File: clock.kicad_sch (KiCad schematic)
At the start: 24 parts, among them SW1 TL2230, U1 LM555, U2 74LS00, U3 LM555

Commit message: Modofied power flags and other minor edits.
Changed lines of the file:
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@@
     (rev "${version}")
-  )
-  (junction (at 107.95 50.8) (diameter 0) (color 0 0 0 0)
   )
   (junction (at 146.05 99.06) (diameter 0) (color 0 0 0 0)
@@
     (stroke (width 0) (type default))
   )
-  (wire (pts (xy 107.95 50.8) (xy 107.95 66.04))
+  (wire (pts (xy 107.95 46.99) (xy 107.95 66.04))
     (stroke (width 0) (type default))
   )
@@
     (stroke (width 0) (type default))
   )
-  (wire (pts (xy 107.95 46.99) (xy 107.95 50.8))
-    (stroke (width 0) (type default))
-  )
   (wire (pts (xy 29.21 81.28) (xy 29.21 104.14))
     (stroke (width 0) (type default))
@@
   )
   (wire (pts (xy 29.21 124.46) (xy 31.75 124.46))
-    (stroke (width 0) (type default))
-  )
-  (wire (pts (xy 107.95 50.8) (xy 110.49 50.8))
     (stroke (width 0) (type default))
   )
@@
         )
       )
-    )
-  )
-  (symbol (lib_id "power:PWR_FLAG") (at 110.49 50.8 270) (unit 1)
-    (in_bom yes) (on_board yes) (dnp no) (fields_autoplaced)
-    (property "Reference" "#FLG01" (at 112.395 50.8 0)
-      (effects (font (size 1 1)) hide)
-    )
-    (property "Value" "PWR_FLAG" (at 113.665 50.8 90)
-      (effects (font (size 1 1)) (justify left))
-    )
-    (property "Footprint" "" (at 110.49 50.8 0)
-      (effects (font (size 1 1)) hide)
-    )
-    (property "Datasheet" "~" (at 110.49 50.8 0)
-      (effects (font (size 1 1)) hide)
-    )
-    (pin "1")
-    (instances
-      (project "cpu"
-        (path "/7aab8e99-eed8-4c64-b2cd-ed9d372ca98a/acfbf03f-1d84-4836-b0c1-074c009b36ca"
-          (reference "#FLG01") (unit 1)
-        )
-      )

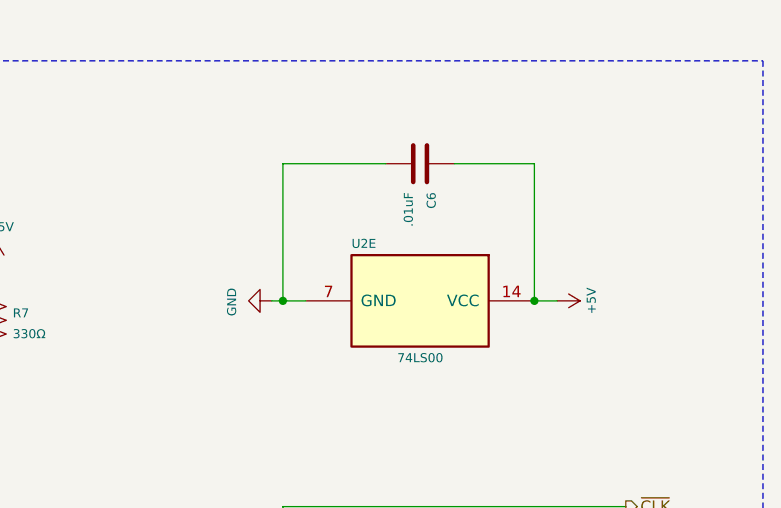
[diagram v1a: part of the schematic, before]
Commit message: Changed out USB connector for new power-only version with fewer pins. Generated new gerber/drill files.
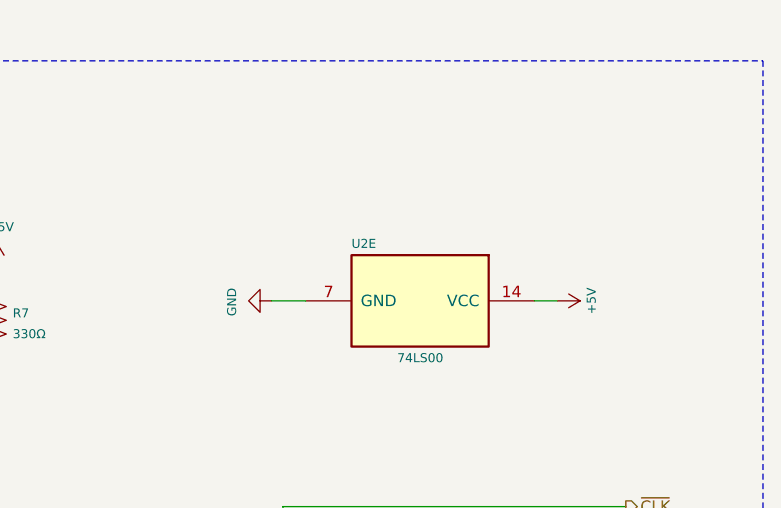
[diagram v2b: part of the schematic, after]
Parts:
- removed C6: .01uF, Capacitor_THT:C_Disc_D4.7mm_W2.5mm_P5.00mm, symbol Device:C
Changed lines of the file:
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@@
   (junction (at 29.21 81.28) (diameter 0) (color 0 0 0 0)
   )
-  (junction (at 237.49 50.8) (diameter 0) (color 0 0 0 0)
-  )
   (junction (at 191.77 134.62) (diameter 0) (color 0 0 0 0)
   )
@@
   )
   (junction (at 34.29 68.58) (diameter 0) (color 0 0 0 0)
-  )
-  (junction (at 209.55 50.8) (diameter 0) (color 0 0 0 0)
   )
   (no_connect (at 134.62 138.43))
@@
     (stroke (width 0) (type default))
   )
-  (wire (pts (xy 208.28 50.8) (xy 209.55 50.8))
+  (wire (pts (xy 208.28 50.8) (xy 212.09 50.8))
     (stroke (width 0) (type default))
   )
@@
     (stroke (width 0) (type default))
   )
-  (wire (pts (xy 220.98 35.56) (xy 209.55 35.56))
-    (stroke (width 0) (type default))
-  )
   (wire (pts (xy 146.05 121.92) (xy 146.05 99.06))
     (stroke (width 0) (type default))
   )
-  (wire (pts (xy 237.49 35.56) (xy 237.49 50.8))
-    (stroke (width 0) (type default))
-  )
   (wire (pts (xy 209.55 73.66) (xy 209.55 91.44))
     (stroke (width 0) (type default))
@@
     (stroke (width 0) (type default))
   )
-  (wire (pts (xy 209.55 50.8) (xy 212.09 50.8))
-    (stroke (width 0) (type default))
-  )
   (wire (pts (xy 69.85 81.28) (xy 72.39 81.28))
     (stroke (width 0) (type default))
@@
     (stroke (width 0) (type default))
   )
-  (wire (pts (xy 228.6 35.56) (xy 237.49 35.56))
-    (stroke (width 0) (type default))
-  )
   (wire (pts (xy 170.18 115.57) (xy 191.77 115.57))
     (stroke (width 0) (type default))
@@
   )
   (wire (pts (xy 191.77 83.82) (xy 191.77 81.28))
-    (stroke (width 0) (type default))
-  )
-  (wire (pts (xy 209.55 35.56) (xy 209.55 50.8))
     (stroke (width 0) (type default))
   )
@@
         )
       )
-    )
-  )
-  (symbol (lib_id "Device:C") (at 224.79 35.56 270) (unit 1)
-    (in_bom yes) (on_board yes) (dnp no) (fields_autoplaced)
-    (property "Reference" "C6" (at 226.06 38.735 0)
-      (effects (font (size 1 1)) (justify left))
-    )
-    (property "Value" ".01uF" (at 223.52 38.735 0)
-      (effects (font (size 1 1)) (justify left))
-    )
-    (property "Footprint" "Capacitor_THT:C_Disc_D4.7mm_W2.5mm_P5.00mm" (at 220.98 36.5252 0)
-      (effects (font (size 1 1)) hide)
-    )
-    (property "Datasheet" "~" (at 224.79 35.56 0)
-      (effects (font (size 1 1)) hide)
-    )
-    (pin "1")
-    (pin "2")
-    (instances
-      (project "cpu"
-        (path "/7aab8e99-eed8-4c64-b2cd-ed9d372ca98a/acfbf03f-1d84-4836-b0c1-074c009b36ca"
-          (reference "C6") (unit 1)
-        )
-      )

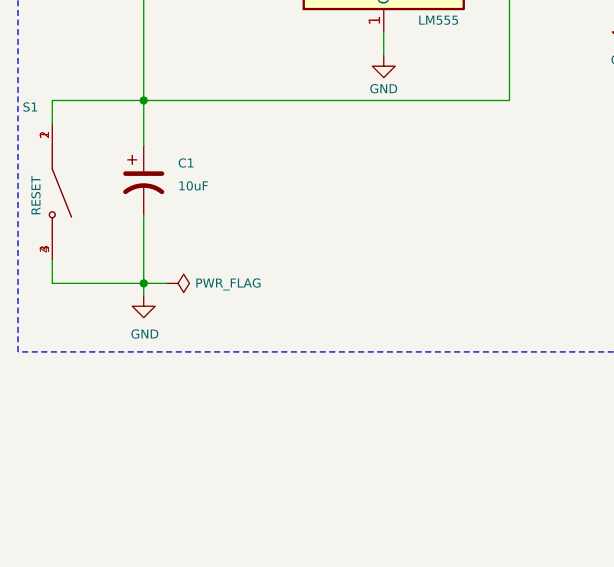
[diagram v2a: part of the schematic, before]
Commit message: Updated symbols/footprint for USB and 5K Trimmer Pots.
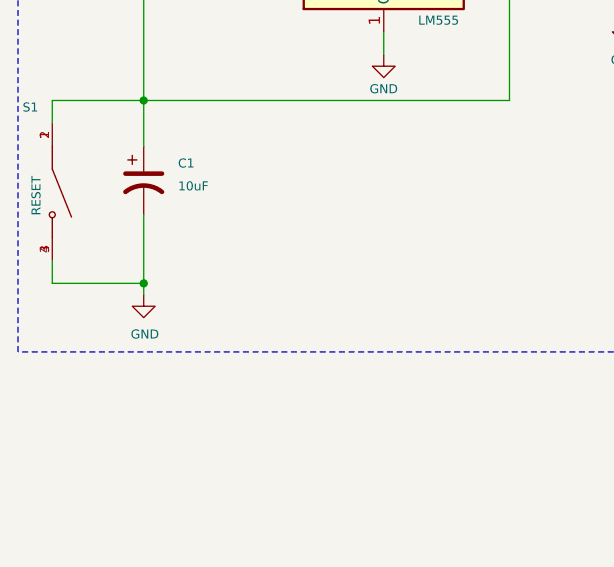
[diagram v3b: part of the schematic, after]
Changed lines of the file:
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@@
-    (stroke (width 0) (type default))
-  )
-  (wire (pts (xy 29.21 124.46) (xy 31.75 124.46))
     (stroke (width 0) (type default))
   )
@@
         )
       )
-    )
-  )
-  (symbol (lib_id "power:PWR_FLAG") (at 31.75 124.46 270) (unit 1)
-    (in_bom yes) (on_board yes) (dnp no) (fields_autoplaced)
-    (property "Reference" "#FLG02" (at 33.655 124.46 0)
-      (effects (font (size 1 1)) hide)
-    )
-    (property "Value" "PWR_FLAG" (at 34.925 124.46 90)
-      (effects (font (size 1 1)) (justify left))
-    )
-    (property "Footprint" "" (at 31.75 124.46 0)
-      (effects (font (size 1 1)) hide)
-    )
-    (property "Datasheet" "~" (at 31.75 124.46 0)
-      (effects (font (size 1 1)) hide)
-    )
-    (pin "1")
-    (instances
-      (project "cpu"
-        (path "/7aab8e99-eed8-4c64-b2cd-ed9d372ca98a/acfbf03f-1d84-4836-b0c1-074c009b36ca"
-          (reference "#FLG02") (unit 1)
-        )
-      )

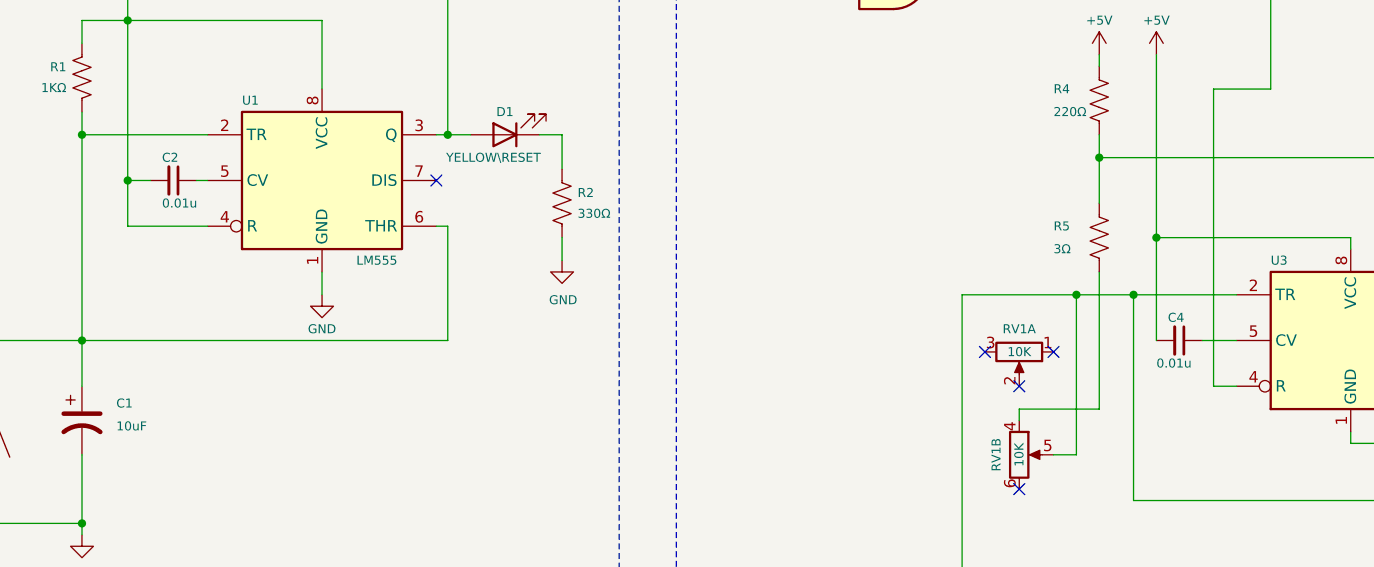
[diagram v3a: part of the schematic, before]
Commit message: Final changes around adding BOM to README.md
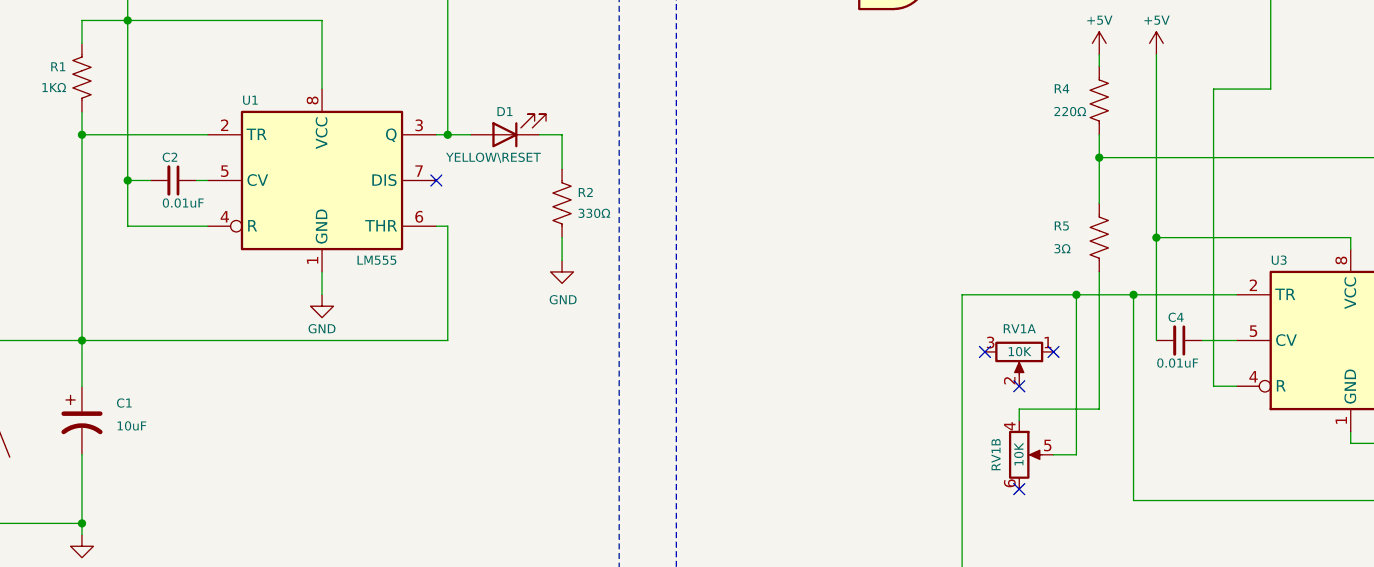
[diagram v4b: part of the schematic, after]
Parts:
- C2, C4: value 0.01u -> 0.01uF
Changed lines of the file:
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@@
       (effects (font (size 1 1)) (justify left))
     )
-    (property "Value" "0.01u" (at 148.59 106.68 90)
+    (property "Value" "0.01uF" (at 148.59 106.68 90)
       (effects (font (size 1 1)) (justify left))
     )
@@
       (effects (font (size 1 1)) (justify left))
     )
-    (property "Value" "0.01u" (at 38.1 88.9 90)
-      (effects (font (size 1 1)) (justify left))
-    )
+    (property "Value" "0.01uF" (at 38.1 88.9 90)
+      (effects (font (size 1 1)) (justify left))
+    )

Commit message: V1.1-last Kicad v7 version
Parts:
- RV1: footprint footprints:10K_Audio_Slide_Pot -> Homebrew-CPU-PCB:10K_Audio_Slide_Pot; symbol homebrew_cpu:R_Potentiometer_Dual_Separate -> Homebrew-CPU-PCB:R_Potentiometer_Dual_Separate
- S1, S2: footprint footprints:SW_1825967-1 -> Homebrew-CPU-PCB:SW_1825967-1; symbol homebrew_cpu:SW-1825967-1 -> Homebrew-CPU-PCB:SW-1825967-1
- SW1: footprint footprints:TL2230EEF140 -> Homebrew-CPU-PCB:TL2230EEF140; symbol homebrew_cpu:TL2230EEF140 -> Homebrew-CPU-PCB:TL2230EEF140
- U1, U3: footprint footprints:DIP-8_W7.62mm_Socket -> Homebrew-CPU-PCB:DIP-8_W7.62mm_Socket; symbol homebrew_cpu:LM555 -> Homebrew-CPU-PCB:LM555
- U2: footprint footprints:DIP-14_W7.62mm_Socket -> Homebrew-CPU-PCB:DIP-14_W7.62mm_Socket; symbol homebrew_cpu:74LS00 -> Homebrew-CPU-PCB:74LS00
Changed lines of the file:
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@@
     )
   )
-  (symbol (lib_id "homebrew_cpu:74LS00") (at 119.38 63.5 0) (unit 1)
+  (symbol (lib_id "Homebrew-CPU-PCB:74LS00") (at 119.38 63.5 0) (unit 1)
     (in_bom yes) (on_board yes) (dnp no)
     (property "Reference" "U2" (at 119.38 55.245 0)
@@
       (effects (font (size 1 1)))
     )
-    (property "Footprint" "footprints:DIP-14_W7.62mm_Socket" (at 119.38 63.5 0)
+    (property "Footprint" "Homebrew-CPU-PCB:DIP-14_W7.62mm_Socket" (at 119.38 63.5 0)
       (effects (font (size 1 1)) hide)
     )
@@
     )
   )
-  (symbol (lib_id "homebrew_cpu:74LS00") (at 226.06 93.98 0) (unit 3)
+  (symbol (lib_name "74LS00_2") (lib_id "Homebrew-CPU-PCB:74LS00") (at 226.06 93.98 0) (unit 3)
     (in_bom yes) (on_board yes) (dnp no)
     (property "Reference" "U2" (at 226.06 85.725 0)
@@
       (effects (font (size 1 1)))
     )
-    (property "Footprint" "footprints:DIP-14_W7.62mm_Socket" (at 226.06 93.98 0)
+    (property "Footprint" "Homebrew-CPU-PCB:DIP-14_W7.62mm_Socket" (at 226.06 93.98 0)
       (effects (font (size 1 1)) hide)
     )
@@
     )
   )
-  (symbol (lib_id "homebrew_cpu:SW-1825967-1") (at 110.49 149.86 0) (unit 1)
+  (symbol (lib_id "Homebrew-CPU-PCB:SW-1825967-1") (at 110.49 149.86 0) (unit 1)
     (in_bom yes) (on_board yes) (dnp no)
     (property "Reference" "S2" (at 102.87 146.558 0)
@@
       (effects (font (size 1 1)) (justify left))
     )
-    (property "Footprint" "footprints:SW_1825967-1" (at 114.3 146.05 0)
+    (property "Footprint" "Homebrew-CPU-PCB:SW_1825967-1" (at 114.3 146.05 0)
       (effects (font (size 1 1)) (justify left bottom) hide)
     )
@@
     )
   )
-  (symbol (lib_id "homebrew_cpu:R_Potentiometer_Dual_Separate") (at 133.35 105.41 270) (unit 1)
+  (symbol (lib_name "R_Potentiometer_Dual_Separate_1") (lib_id "Homebrew-CPU-PCB:R_Potentiometer_Dual_Separate") (at 133.35 105.41 270) (unit 1)
     (in_bom yes) (on_board yes) (dnp no)
     (property "Reference" "RV1" (at 133.35 102.87 90)
@@
       (effects (font (size 1 1)))
     )
-    (property "Footprint" "footprints:10K_Audio_Slide_Pot" (at 133.35 105.41 0)
+    (property "Footprint" "Homebrew-CPU-PCB:10K_Audio_Slide_Pot" (at 133.35 105.41 0)
       (effects (font (size 1 1)) hide)
     )
@@
     )
   )
-  (symbol (lib_id "homebrew_cpu:74LS00") (at 224.79 50.8 270) (unit 5)
+  (symbol (lib_id "Homebrew-CPU-PCB:74LS00") (at 224.79 50.8 270) (unit 5)
     (in_bom yes) (on_board yes) (dnp no)
     (property "Reference" "U2" (at 217.17 44.45 90)
@@
       (effects (font (size 1 1)) (justify left))
     )
-    (property "Footprint" "footprints:DIP-14_W7.62mm_Socket" (at 224.79 50.8 0)
-      (effects (font (size 1 1)) hide)
+    (property "Footprint" "Homebrew-CPU-PCB:DIP-14_W7.62mm_Socket" (at 224.79 50.8 0)
+      (effects (font (size 1.27 1.27)) hide)
     )
     (property "Datasheet" "http://www.ti.com/lit/gpn/sn74ls00" (at 224.79 50.8 0)
-      (effects (font (size 1 1)) hide)
+      (effects (font (size 1.27 1.27)) hide)
     )
     (pin "9")
@@
     )
   )
-  (symbol (lib_name "TL2230EEF140_1") (lib_id "homebrew_cpu:TL2230EEF140") (at 134.62 138.43 0) (unit 1)
+  (symbol (lib_id "Homebrew-CPU-PCB:TL2230EEF140") (at 134.62 138.43 0) (unit 1)
     (in_bom yes) (on_board yes) (dnp no)
     (property "Reference" "SW1" (at 140.97 134.62 0)
@@
       (effects (font (size 1 1)))
     )
-    (property "Footprint" "footprints:TL2230EEF140" (at 161.29 233.35 0)
+    (property "Footprint" "Homebrew-CPU-PCB:TL2230EEF140" (at 161.29 233.35 0)
       (effects (font (size 1 1)) (justify left top) hide)
     )
@@
     )
   )
-  (symbol (lib_id "homebrew_cpu:R_Potentiometer_Dual_Separate") (at 133.35 116.84 0) (unit 2)
+  (symbol (lib_id "Homebrew-CPU-PCB:R_Potentiometer_Dual_Separate") (at 133.35 116.84 0) (unit 2)
     (in_bom yes) (on_board yes) (dnp no)
     (property "Reference" "RV1" (at 130.81 116.84 90)
@@
       (effects (font (size 1 1)))
     )
-    (property "Footprint" "footprints:10K_Audio_Slide_Pot" (at 133.35 116.84 0)
+    (property "Footprint" "Homebrew-CPU-PCB:10K_Audio_Slide_Pot" (at 133.35 116.84 0)
       (effects (font (size 1 1)) hide)
     )
@@
     )
   )
-  (symbol (lib_id "homebrew_cpu:LM555") (at 170.18 104.14 0) (unit 1)
+  (symbol (lib_id "Homebrew-CPU-PCB:LM555") (at 170.18 104.14 0) (unit 1)
     (in_bom yes) (on_board yes) (dnp no)
     (property "Reference" "U3" (at 161.29 95.25 0)
@@
       (effects (font (size 1 1)) (justify left))
     )
-    (property "Footprint" "footprints:DIP-8_W7.62mm_Socket" (at 186.69 114.3 0)
+    (property "Footprint" "Homebrew-CPU-PCB:DIP-8_W7.62mm_Socket" (at 186.69 114.3 0)
       (effects (font (size 1 1)) hide)
     )
@@
     )
   )
-  (symbol (lib_id "homebrew_cpu:74LS00") (at 203.2 96.52 0) (mirror x) (unit 4)
+  (symbol (lib_name "74LS00_1") (lib_id "Homebrew-CPU-PCB:74LS00") (at 203.2 96.52 0) (mirror x) (unit 4)
     (in_bom yes) (on_board yes) (dnp no)
     (property "Reference" "U2" (at 203.2 104.775 0)
@@
       (effects (font (size 1 1)))
     )
-    (property "Footprint" "footprints:DIP-14_W7.62mm_Socket" (at 203.2 96.52 0)
+    (property "Footprint" "Homebrew-CPU-PCB:DIP-14_W7.62mm_Socket" (at 203.2 96.52 0)
       (effects (font (size 1 1)) hide)
     )
@@
     )
   )
-  (symbol (lib_id "homebrew_cpu:74LS00") (at 149.86 60.96 0) (unit 2)
+  (symbol (lib_name "74LS00_4") (lib_id "Homebrew-CPU-PCB:74LS00") (at 149.86 60.96 0) (unit 2)
     (in_bom yes) (on_board yes) (dnp no)
     (property "Reference" "U2" (at 149.86 52.705 0)
@@
       (effects (font (size 1 1)))
     )
-    (property "Footprint" "footprints:DIP-14_W7.62mm_Socket" (at 149.86 60.96 0)
+    (property "Footprint" "Homebrew-CPU-PCB:DIP-14_W7.62mm_Socket" (at 149.86 60.96 0)
       (effects (font (size 1 1)) hide)
     )
@@
     )
   )
-  (symbol (lib_id "homebrew_cpu:LM555") (at 55.88 86.36 0) (unit 1)
+  (symbol (lib_name "LM555_1") (lib_id "Homebrew-CPU-PCB:LM555") (at 55.88 86.36 0) (unit 1)
     (in_bom yes) (on_board yes) (dnp no)
     (property "Reference" "U1" (at 46.99 77.47 0)
@@
       (effects (font (size 1 1)) (justify left))
     )
-    (property "Footprint" "footprints:DIP-8_W7.62mm_Socket" (at 72.39 96.52 0)
+    (property "Footprint" "Homebrew-CPU-PCB:DIP-8_W7.62mm_Socket" (at 72.39 96.52 0)
       (effects (font (size 1 1)) hide)
     )
@@
     )
   )
-  (symbol (lib_id "homebrew_cpu:SW-1825967-1") (at 19.05 114.3 270) (unit 1)
+  (symbol (lib_name "SW-1825967-1_1") (lib_id "Homebrew-CPU-PCB:SW-1825967-1") (at 19.05 114.3 270) (unit 1)
     (in_bom yes) (on_board yes) (dnp no)
     (property "Reference" "S1" (at 15.748 104.902 90)
@@
       (effects (font (size 1 1)) (justify left))
     )
-    (property "Footprint" "footprints:SW_1825967-1" (at 22.86 118.11 0)
+    (property "Footprint" "Homebrew-CPU-PCB:SW_1825967-1" (at 22.86 118.11 0)
       (effects (font (size 1 1)) (justify left bottom) hide)
     )

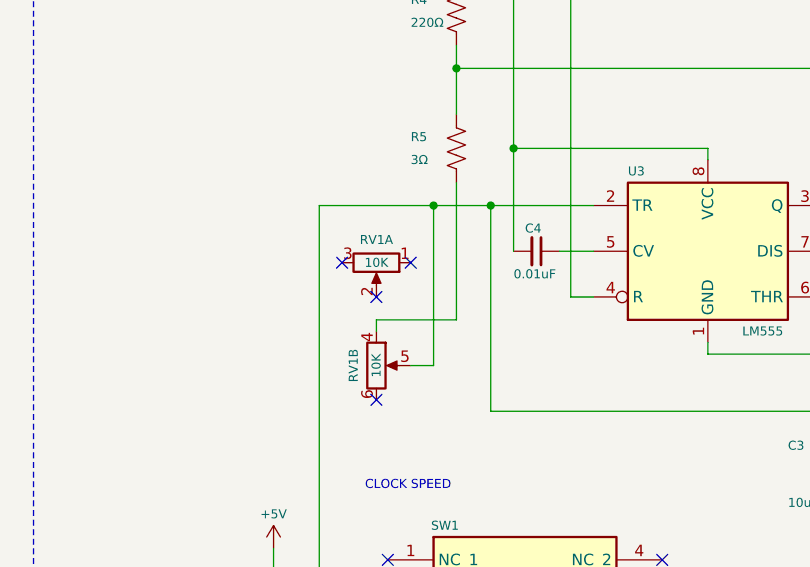
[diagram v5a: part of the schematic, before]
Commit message: First KiCad v8 version.All ERC/DRC errors/warnings fixed - had to fix nets on left end of audio potentiometer so that they match. Weird.
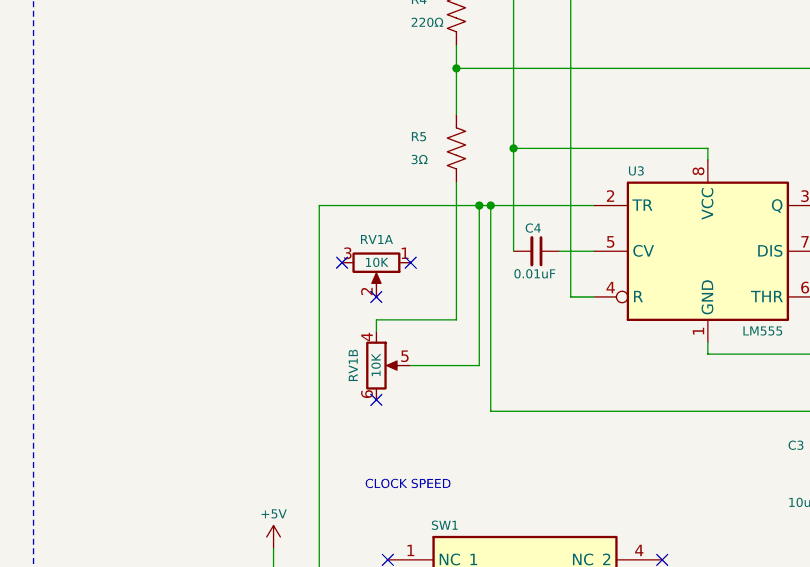
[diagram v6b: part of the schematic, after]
